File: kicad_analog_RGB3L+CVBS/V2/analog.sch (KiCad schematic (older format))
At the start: 24 parts, among them P1 Conn_02x05_Odd_Even, P2 Conn_01x04, P3 Conn_01x05, P4 Conn_01x02, P6 Conn_01x01, P7 Conn_01x01, U1 MAX9144, U2 MAX9144, U3 4066, U4 MCP1754S-3302xCB, U5 MAX5259EEE+

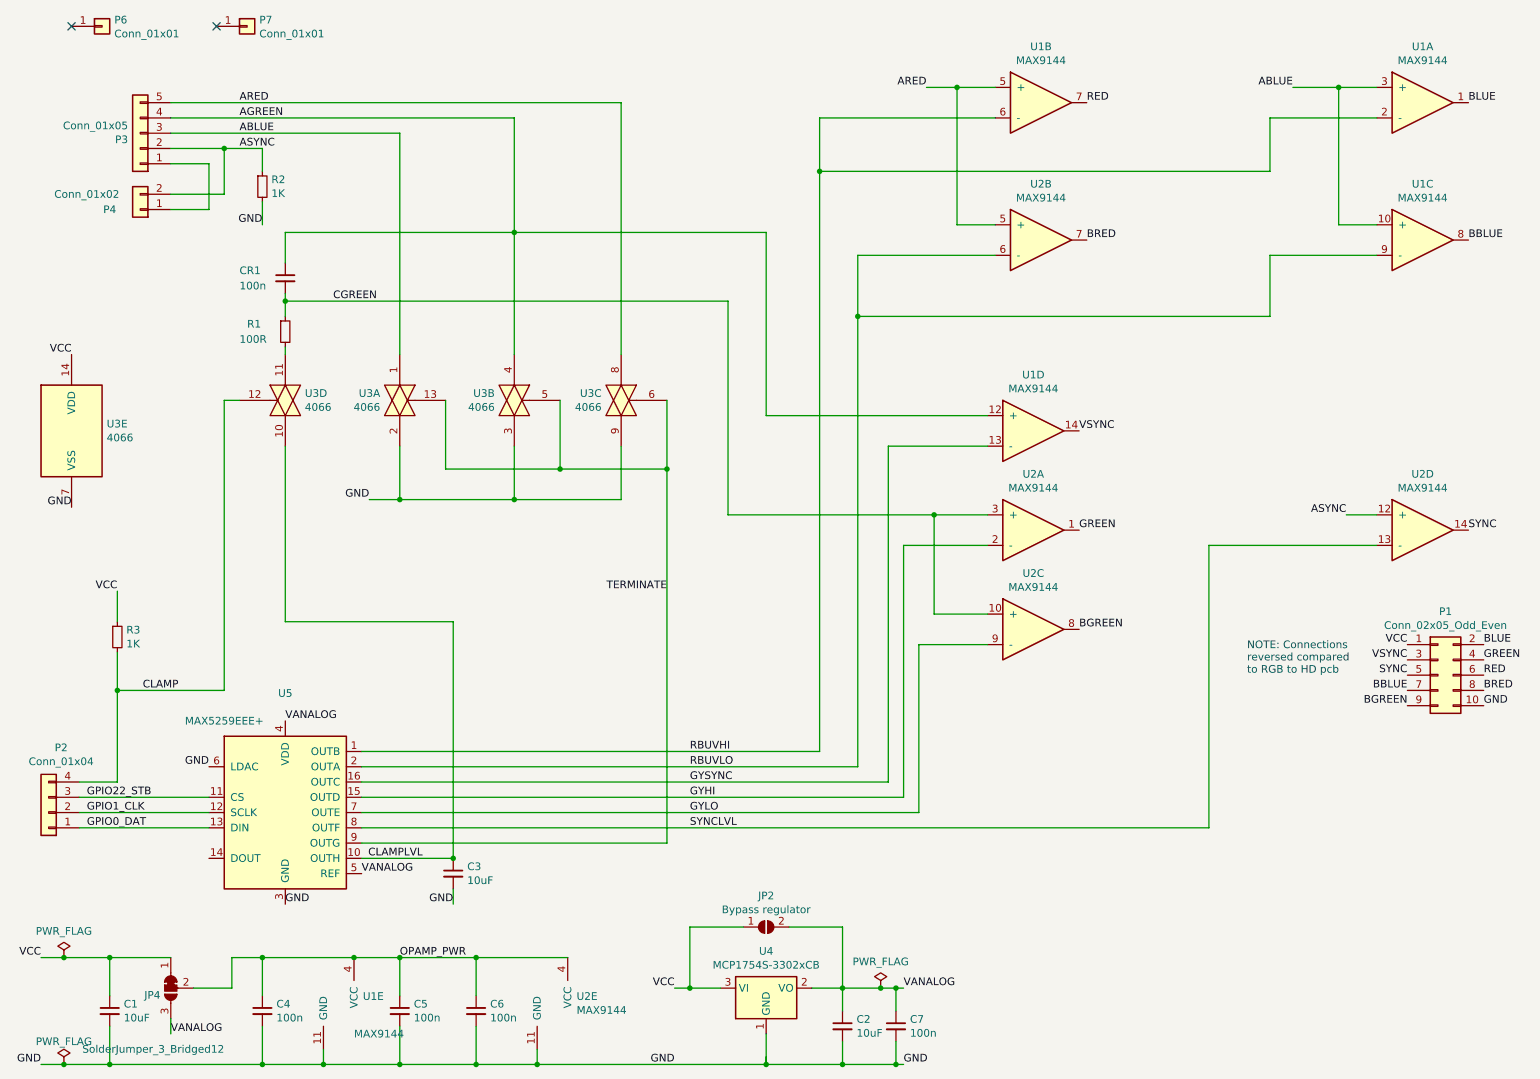
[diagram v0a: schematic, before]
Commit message: Terminator and decoupling caps added plus pcb layout
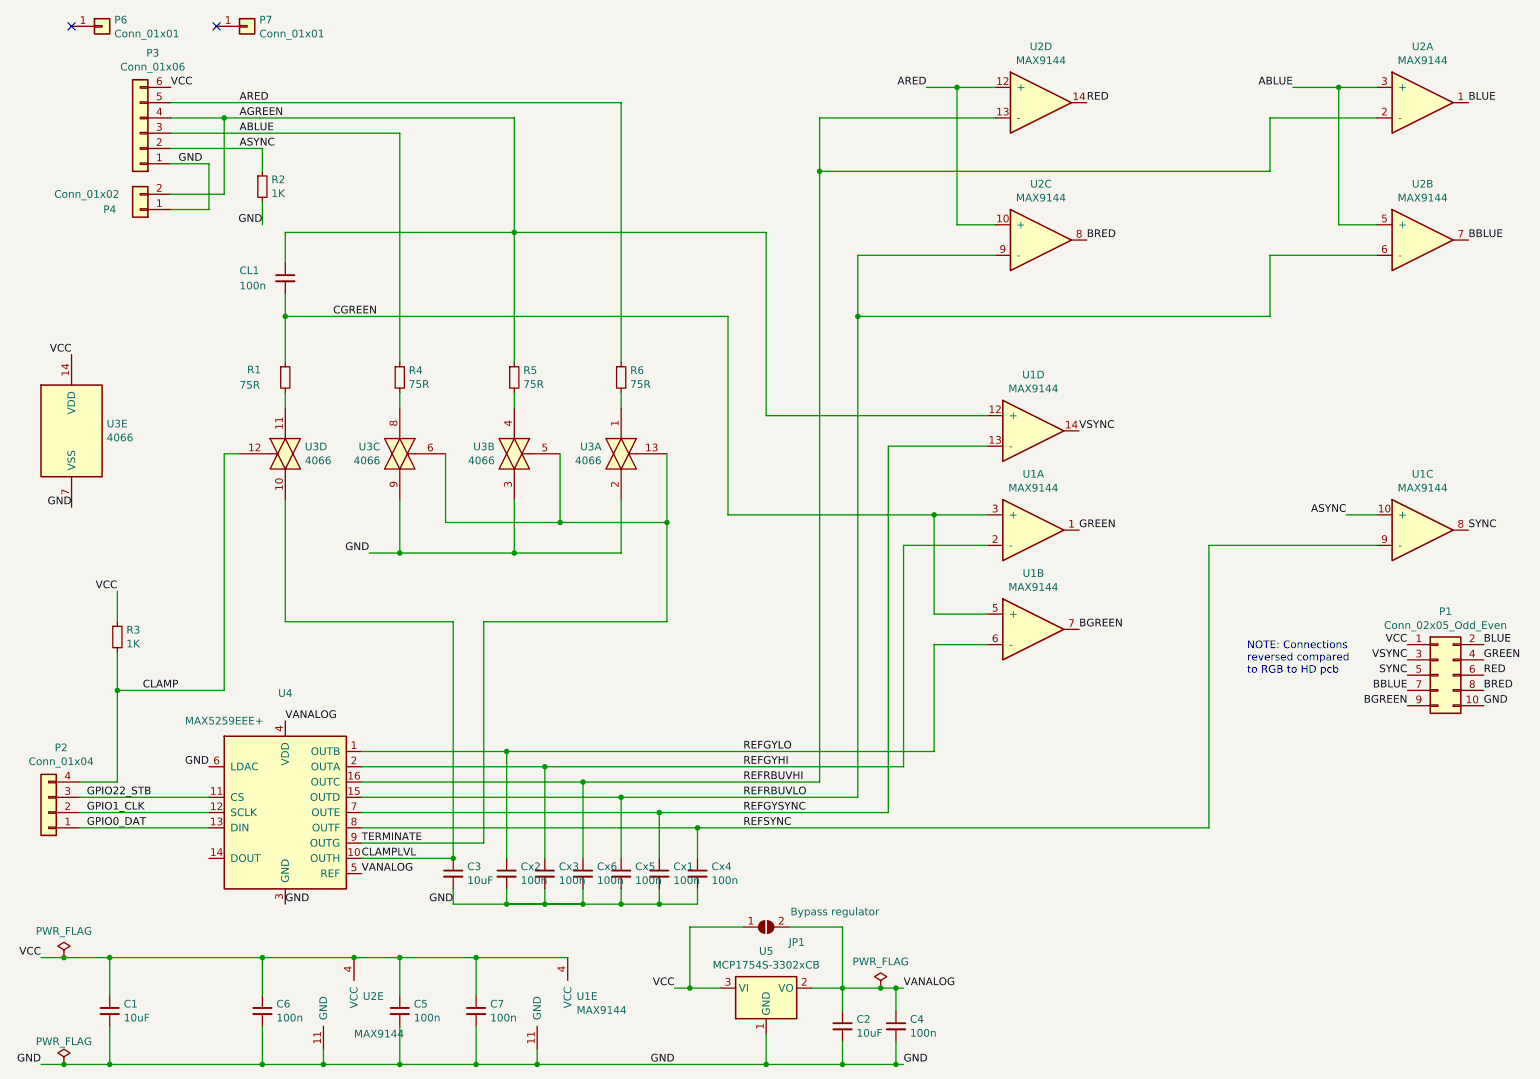
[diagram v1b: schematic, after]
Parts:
- removed JP4: SolderJumper_3_Bridged12, Jumper:SolderJumper-3_P1.3mm_Bridged12_RoundedPad1.0x1.5mm_NumberLabels, symbol Jumper:SolderJumper_3_Bridged12
- removed P3: Conn_01x05, Connector_Molex:Molex_PicoBlade_53048-0510_1x05_P1.25mm_Horizontal, symbol Connector_Generic:Conn_01x05
- added Cx1, Cx2, Cx3, Cx4, Cx5, Cx6: 100n, Capacitor_SMD:C_0805_2012Metric_Pad1.15x1.40mm_HandSolder, symbol Device:C_Small
- added P3: Conn_01x06, Connector_Molex:Molex_PicoBlade_53048-0610_1x06_P1.25mm_Horizontal, symbol Connector_Generic:Conn_01x06
- added R4, R5, R6: 75R, Resistor_SMD:R_0805_2012Metric_Pad1.15x1.40mm_HandSolder, symbol Device:R_Small
- R1: value 100R -> 75R; footprint (none) -> Resistor_SMD:R_0805_2012Metric_Pad1.15x1.40mm_HandSolder
- renumbered C7 to C4, C4 to C6, C6 to C7, CR1 to CL1, JP2 to JP1, U2 to U1, U1 to U2, U5 to U4, U4 to U5
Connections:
- net OPAMP_PWR is gone; now on net VCC: C5.1, C6.1, C7.1, U1.4 (VCC), U2.4 (VCC)
- net ABLUE: now also U2.5 (+), P3.3 (Pin_3), R4.1; no longer U2.10 (+), U3.1
- net AGREEN: now also P4.2 (Pin_2), U1.12 (+), P3.4 (Pin_4), R5.1; no longer U2.12 (+), U3.4
- net ARED: now also U2.10 (+), U2.12 (+), P3.5 (Pin_5), R6.1; no longer U1.5 (+), U2.5 (+), U3.8
- net ASYNC: now also U1.10 (+), P3.2 (Pin_2); no longer P4.2 (Pin_2), U1.12 (+)
- net BBLUE: now also U2.7; no longer U2.8
- net BGREEN: now also U1.7; no longer U1.8
- net BRED: now also U2.8; no longer U1.7
- net CGREEN: now also U1.5 (+); no longer U1.10 (+)
- net GND: now also P4.1 (Pin_1), Cx1.2, Cx2.2, Cx3.2, Cx4.2, Cx5.2, Cx6.2, P3.1 (Pin_1)
- net RED: now also U2.14; no longer U2.7
- net SYNC: now also U1.8; no longer U1.14
- net VCC: now also P3.6 (Pin_6)
- net VSYNC: now also U1.14; no longer U2.14
- net GYHI renamed REFGYHI
- net REFGYHI: now also U4.2 (OUTA), Cx3.1; no longer U4.15 (OUTD)
- net GYLO renamed REFGYSYNC
- net REFGYSYNC: now also U1.13 (-), Cx1.1; no longer U1.9 (-)
- net GYSYNC renamed REFRBUVHI
- net REFRBUVHI: now also U2.2 (-), Cx6.1
- removed net RBUVHI: U2.2 (-), U2.6 (-), U4.1 (OUTB)
- removed net RBUVLO: U1.6 (-), U2.9 (-), U4.2 (OUTA)
- net SYNCLVL renamed REFSYNC
- net REFSYNC: now also U1.9 (-), Cx4.1; no longer U1.13 (-)
- new net: R4.2, U3.8
- new net: R5.2, U3.4
- new net: R6.2, U3.1
- new net REFGYLO: Cx2.1, U1.6 (-), U4.1 (OUTB)
- new net REFRBUVLO: Cx5.1, U2.6 (-), U2.9 (-), U4.15 (OUTD)
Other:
- moved on the sheet: R1, U1B, U1C, U1D, U2B, U2C, U2D, U3A, U3B, U3C, U3D
